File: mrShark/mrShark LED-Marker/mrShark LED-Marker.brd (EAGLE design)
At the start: 26 x 31 mm, 38 parts, among them CON1 DF12-20DS, IC1 PCA9552PW

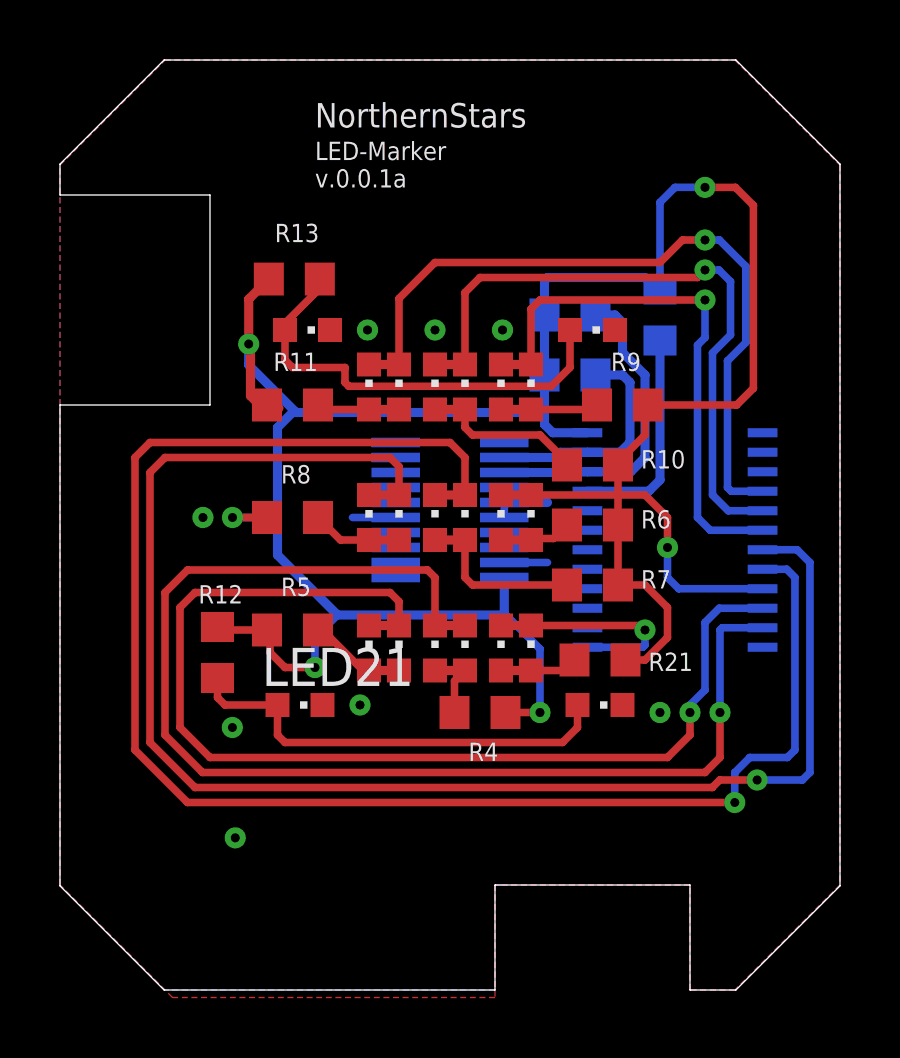
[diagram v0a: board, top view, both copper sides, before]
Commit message: Updated LED-marker to version 0.0.1
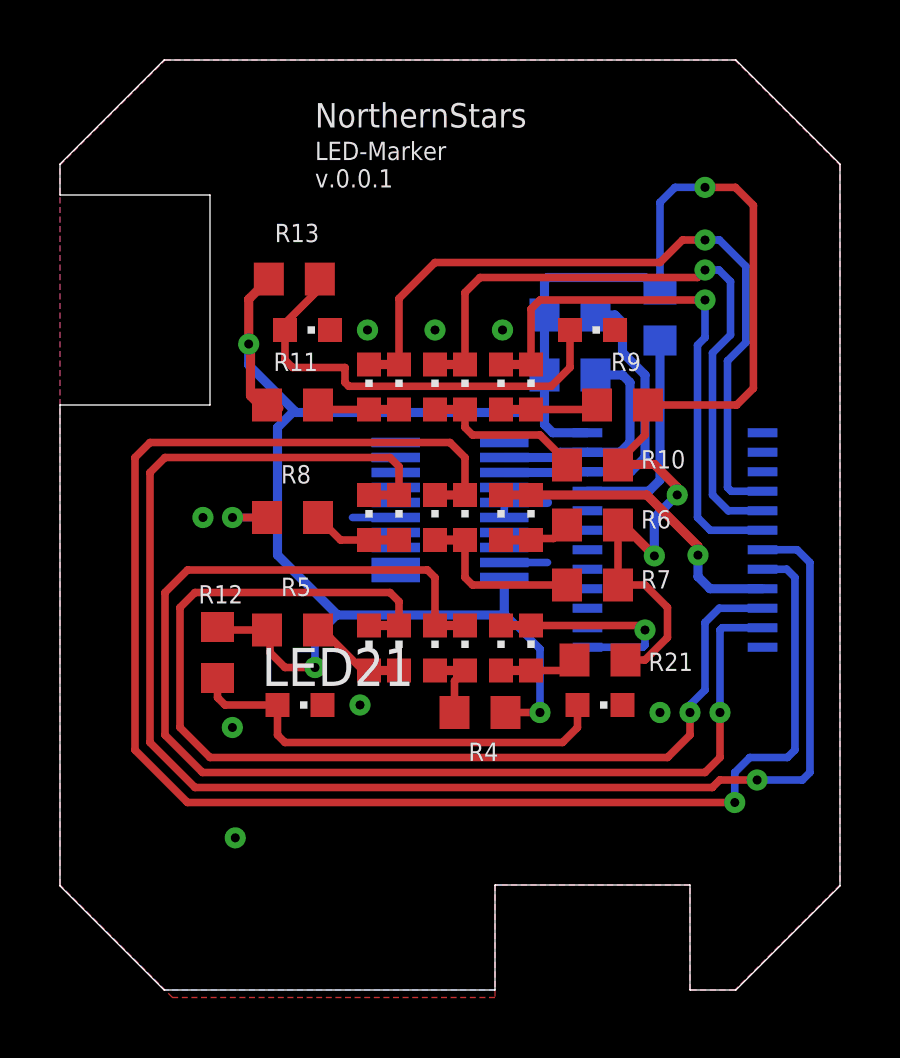
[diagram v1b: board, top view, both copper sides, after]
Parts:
- LED2: value (none) -> LW L283
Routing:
- net VCC: track 83.5 -> 88.0 mm, vias 5 -> 7
- net N$18: track 11.2 -> 10.6 mm
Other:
- board text added: "LED-Marker v.0.0.1"
- board text removed: "LED-Marker v.0.0.1a"
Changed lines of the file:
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@@
 <text x="8.5" y="28.25" size="0.8128" layer="25" font="vector" ratio="15">NorthernStars</text>
 <text x="8.5" y="26.25" size="0.6096" layer="25" font="vector" ratio="15">LED-Marker
-v.0.0.1a</text>
+v.0.0.1</text>
 <wire x1="5" y1="26" x2="5" y2="19" width="0" layer="20"/>
 <wire x1="0" y1="26" x2="5" y2="26" width="0" layer="20"/>
@@
 <attribute name="VALUE" x="12.205" y="18.33" size="1.27" layer="27" rot="R90"/>
 </element>
-<element name="LED2" library="led" package="CHIPLED_0603" value="" x="11.3" y="19.6" smashed="yes">
+<element name="LED2" library="led" package="CHIPLED_0603" value="LW L283" x="11.3" y="19.6" smashed="yes">
 <attribute name="VALUE" x="13.205" y="18.33" size="1.27" layer="27" rot="R90"/>
 </element>
@@
 <wire x1="5.75" y1="15.25" x2="7.25" y2="15.25" width="0.254" layer="16"/>
 <via x="6.29" y="21.032" extent="1-16" drill="0.3" shape="octagon"/>
-<wire x1="18.6" y1="15" x2="18.6" y2="17" width="0.254" layer="1"/>
 <wire x1="18.6" y1="13" x2="18.6" y2="15" width="0.254" layer="1"/>
 <via x="21.5" y="26.254" extent="1-16" drill="0.3" shape="octagon"/>
@@
 <wire x1="23.114" y1="25.654" x2="22.514" y2="26.254" width="0.254" layer="1"/>
 <wire x1="21.5" y1="26.254" x2="22.514" y2="26.254" width="0.254" layer="1"/>
+<wire x1="18.6" y1="15" x2="18.782" y2="15" width="0.3048" layer="1"/>
+<wire x1="18.782" y1="15" x2="19.812" y2="13.97" width="0.3048" layer="1"/>
+<via x="19.812" y="13.97" extent="1-16" drill="0.3" shape="octagon"/>
+<wire x1="19.812" y1="13.97" x2="19.812" y2="15.24" width="0.3048" layer="16"/>
+<wire x1="19.812" y1="15.24" x2="20.574" y2="16.002" width="0.3048" layer="16"/>
+<via x="20.574" y="16.002" extent="1-16" drill="0.3" shape="octagon"/>
+<wire x1="20.574" y1="16.002" x2="20.574" y2="16.256" width="0.3048" layer="1"/>
+<wire x1="20.574" y1="16.256" x2="19.812" y2="17.018" width="0.3048" layer="1"/>
+<wire x1="19.812" y1="17.018" x2="18.618" y2="17.018" width="0.3048" layer="1"/>
+<wire x1="18.618" y1="17.018" x2="18.6" y2="17" width="0.3048" layer="1"/>
 </signal>
 <signal name="GND">
@@
 <contactref element="LED11" pad="C"/>
 <wire x1="14.7" y1="16" x2="15.7" y2="16" width="0.3048" layer="1"/>
-<wire x1="15.7" y1="16" x2="19.5" y2="16" width="0.254" layer="1"/>
-<via x="20.25" y="14.25" extent="1-16" drill="0.3" shape="octagon"/>
-<wire x1="20.25" y1="13.25" x2="20.625" y2="12.875" width="0.254" layer="16"/>
-<wire x1="23.4178" y1="12.875" x2="20.625" y2="12.875" width="0.254" layer="16"/>
-<wire x1="20.25" y1="13.25" x2="20.25" y2="14.25" width="0.254" layer="16"/>
-<wire x1="20.25" y1="14.25" x2="20.25" y2="15.25" width="0.254" layer="1"/>
-<wire x1="20.25" y1="15.25" x2="19.5" y2="16" width="0.254" layer="1"/>
+<via x="21.266" y="13.996" extent="1-16" drill="0.3" shape="octagon"/>
+<wire x1="23.4178" y1="12.875" x2="21.669" y2="12.875" width="0.3048" layer="16"/>
+<wire x1="15.7" y1="16" x2="19.56" y2="16" width="0.3048" layer="1"/>
+<wire x1="19.56" y1="16" x2="21.266" y2="14.294" width="0.3048" layer="1"/>
+<wire x1="21.266" y1="14.294" x2="21.266" y2="13.996" width="0.3048" layer="1"/>
+<wire x1="21.669" y1="12.875" x2="21.266" y2="13.278" width="0.3048" layer="16"/>
+<wire x1="21.266" y1="13.278" x2="21.266" y2="13.996" width="0.3048" layer="16"/>
 </signal>
 <signal name="N$19">

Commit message: Updated LED-marker
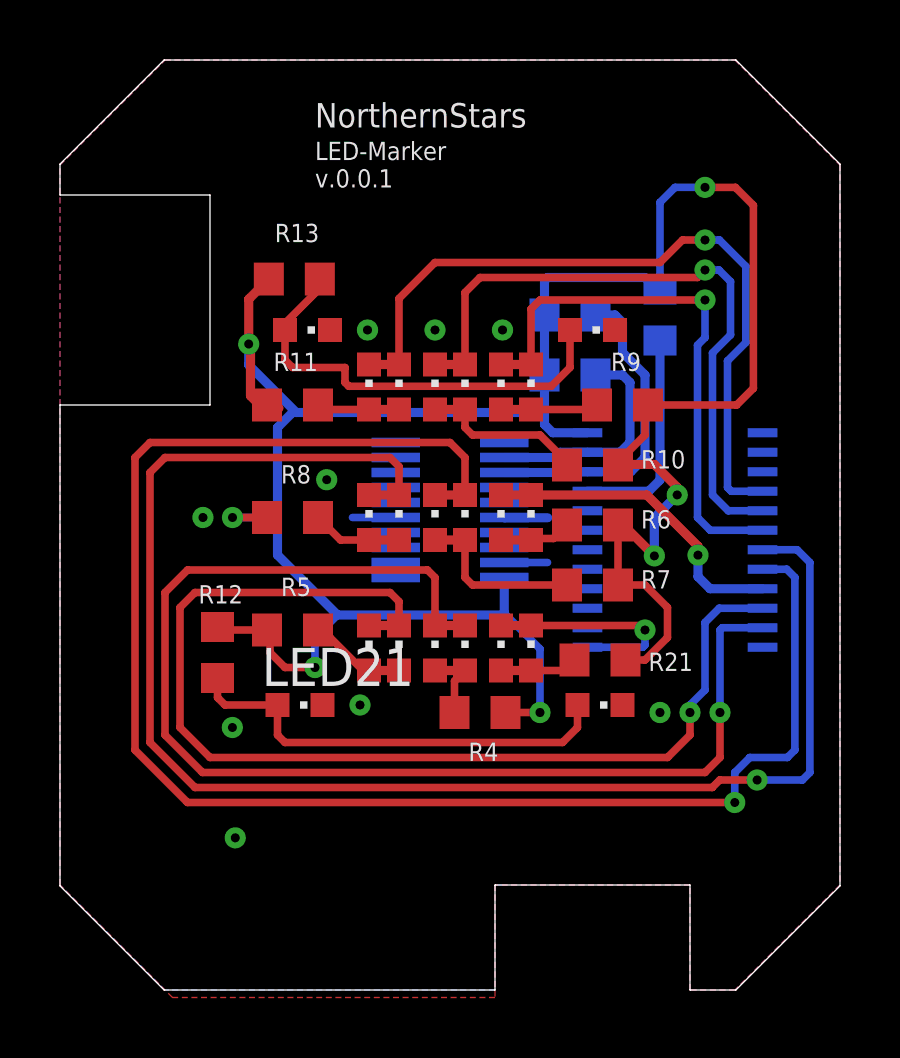
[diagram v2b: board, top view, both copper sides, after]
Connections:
- net GND: no longer CON1.16
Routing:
- net GND: track 4.82 -> 4.33 mm, vias 8 -> 9
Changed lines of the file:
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@@
 <signal name="GND">
 <contactref element="CON1" pad="15"/>
-<contactref element="CON1" pad="16"/>
 <contactref element="CON1" pad="12"/>
 <contactref element="CON1" pad="6"/>
@@
 <vertex x="3.75" y="-0.75"/>
 </polygon>
-<wire x1="14.81" y1="15.75" x2="16.25" y2="15.75" width="0.3048" layer="16"/>
 <contactref element="LED20" pad="C"/>
 <contactref element="LED19" pad="C"/>
@@
 <contactref element="LED21" pad="C"/>
 <wire x1="14.81" y1="13.75" x2="16.25" y2="13.75" width="0.254" layer="16"/>
-<wire x1="14.81" y1="15.25" x2="14.81" y2="15.75" width="0.254" layer="16"/>
 <via x="10.25" y="21.5" extent="1-16" drill="0.3" shape="octagon"/>
 <via x="10" y="9" extent="1-16" drill="0.3" shape="octagon"/>
@@
 <via x="5.746" y="8.25" extent="1-16" drill="0.3" shape="octagon"/>
 <via x="5.842" y="4.572" extent="1-16" drill="0.3" shape="octagon"/>
-<wire x1="11.19" y1="15.25" x2="14.81" y2="15.25" width="0" layer="19" extent="16-16"/>
+<wire x1="14.81" y1="15.25" x2="14.82" y2="15.24" width="0.3048" layer="16"/>
+<wire x1="14.82" y1="15.24" x2="16.256" y2="15.24" width="0.3048" layer="16"/>
+<via x="8.89" y="16.51" extent="1-16" drill="0.3" shape="octagon"/>
 </signal>
 <signal name="INT1">

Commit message: Added switchable position lights
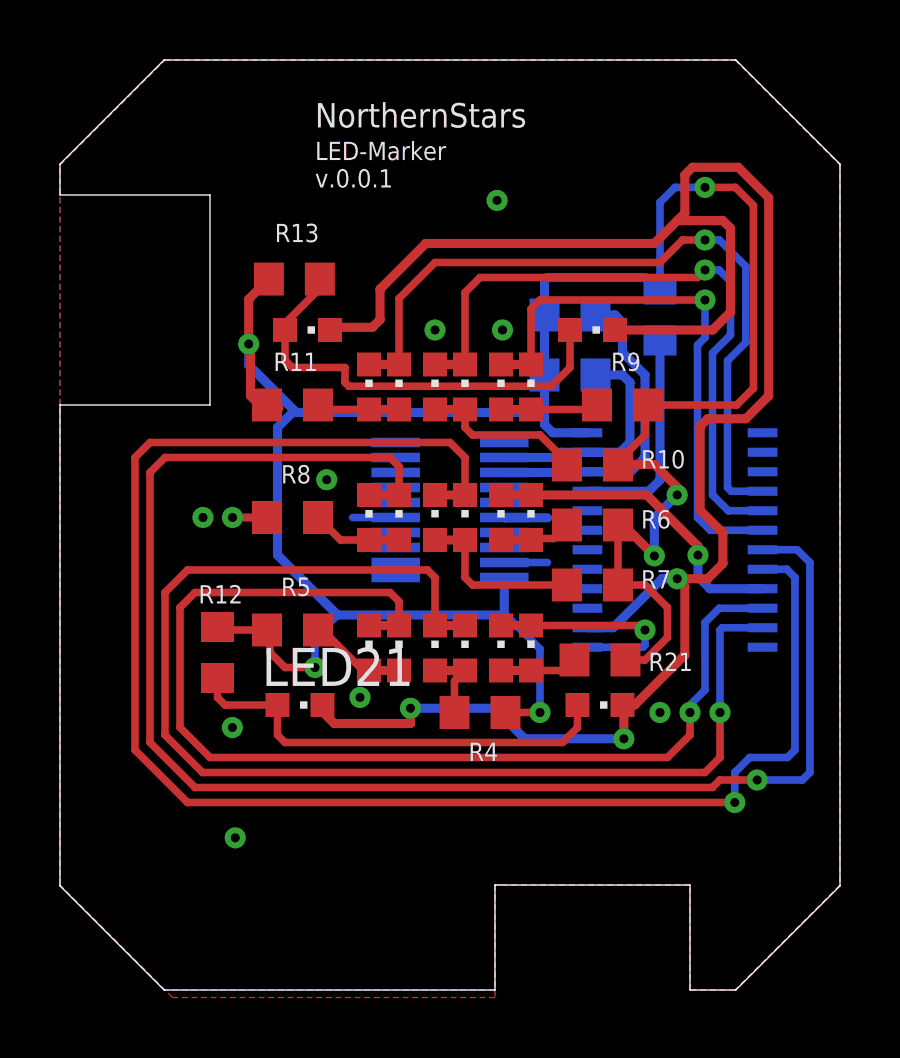
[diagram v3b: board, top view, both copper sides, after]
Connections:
- new net POS_LIGHT: IC1.14, LED19.C, LED20.C, LED21.C, LED22.C
- net GND: no longer LED19.C, LED20.C, LED21.C, LED22.C
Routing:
- net POS_LIGHT: track 0.00 -> 64.9 mm, vias 0 -> 3
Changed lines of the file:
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@@
 <vertex x="3.75" y="-0.75"/>
 </polygon>
-<contactref element="LED20" pad="C"/>
-<contactref element="LED19" pad="C"/>
-<contactref element="LED22" pad="C"/>
-<contactref element="LED21" pad="C"/>
 <wire x1="14.81" y1="13.75" x2="16.25" y2="13.75" width="0.254" layer="16"/>
-<via x="10.25" y="21.5" extent="1-16" drill="0.3" shape="octagon"/>
-<via x="10" y="9" extent="1-16" drill="0.3" shape="octagon"/>
+<via x="14.568" y="25.818" extent="1-16" drill="0.3" shape="octagon"/>
+<via x="10" y="9.254" extent="1-16" drill="0.3" shape="octagon"/>
 <wire x1="11.19" y1="15.25" x2="9.75" y2="15.25" width="0.254" layer="16"/>
 <via x="20" y="8.75" extent="1-16" drill="0.3" shape="octagon"/>
@@
 <wire x1="8.662" y1="22.886" x2="8.662" y2="23.198" width="0.254" layer="1"/>
 </signal>
+<signal name="POS_LIGHT">
+<contactref element="IC1" pad="14"/>
+<contactref element="LED20" pad="C"/>
+<contactref element="LED19" pad="C"/>
+<contactref element="LED22" pad="C"/>
+<contactref element="LED21" pad="C"/>
+<wire x1="17.5822" y1="11.575" x2="18.433" y2="11.575" width="0.3048" layer="16"/>
+<wire x1="18.433" y1="11.575" x2="20.066" y2="13.208" width="0.3048" layer="16"/>
+<wire x1="8.75" y1="9" x2="8.75" y2="8.776" width="0.3048" layer="1"/>
+<wire x1="8.75" y1="8.776" x2="9.144" y2="8.382" width="0.3048" layer="1"/>
+<wire x1="9.144" y1="8.382" x2="11.684" y2="8.382" width="0.3048" layer="1"/>
+<wire x1="11.684" y1="8.382" x2="11.684" y2="8.89" width="0.3048" layer="1"/>
+<via x="11.684" y="8.89" extent="1-16" drill="0.3" shape="octagon"/>
+<wire x1="11.684" y1="8.89" x2="14.478" y2="8.89" width="0.3048" layer="16"/>
+<wire x1="14.478" y1="8.89" x2="15.494" y2="7.874" width="0.3048" layer="16"/>
+<wire x1="15.494" y1="7.874" x2="18.796" y2="7.874" width="0.3048" layer="16"/>
+<via x="18.796" y="7.874" extent="1-16" drill="0.3" shape="octagon"/>
+<wire x1="18.796" y1="7.874" x2="18.796" y2="8.954" width="0.3048" layer="1"/>
+<wire x1="18.796" y1="8.954" x2="18.75" y2="9" width="0.3048" layer="1"/>
+<wire x1="18.5" y1="21.5" x2="21.754" y2="21.5" width="0.3048" layer="1"/>
+<wire x1="21.754" y1="21.5" x2="22.352" y2="22.098" width="0.3048" layer="1"/>
+<wire x1="22.352" y1="22.098" x2="22.352" y2="24.892" width="0.3048" layer="1"/>
+<wire x1="22.352" y1="24.892" x2="22.098" y2="25.146" width="0.3048" layer="1"/>
+<wire x1="22.098" y1="25.146" x2="20.574" y2="25.146" width="0.3048" layer="1"/>
+<wire x1="20.574" y1="25.146" x2="19.812" y2="24.384" width="0.3048" layer="1"/>
+<wire x1="19.812" y1="24.384" x2="12.192" y2="24.384" width="0.3048" layer="1"/>
+<wire x1="12.192" y1="24.384" x2="10.668" y2="22.86" width="0.3048" layer="1"/>
+<wire x1="10.668" y1="22.86" x2="10.668" y2="21.844" width="0.3048" layer="1"/>
+<wire x1="10.668" y1="21.844" x2="10.414" y2="21.59" width="0.3048" layer="1"/>
+<wire x1="10.414" y1="21.59" x2="9.09" y2="21.59" width="0.3048" layer="1"/>
+<wire x1="9.09" y1="21.59" x2="9" y2="21.5" width="0.3048" layer="1"/>
+<wire x1="22.098" y1="13.716" x2="22.098" y2="14.732" width="0.3048" layer="1"/>
+<wire x1="22.098" y1="14.732" x2="21.336" y2="15.494" width="0.3048" layer="1"/>
+<wire x1="21.336" y1="15.494" x2="21.336" y2="18.288" width="0.3048" layer="1"/>
+<wire x1="21.336" y1="18.288" x2="21.59" y2="18.542" width="0.3048" layer="1"/>
+<wire x1="21.59" y1="18.542" x2="22.86" y2="18.542" width="0.3048" layer="1"/>
+<wire x1="22.86" y1="18.542" x2="23.622" y2="19.304" width="0.3048" layer="1"/>
+<wire x1="23.622" y1="19.304" x2="23.622" y2="25.908" width="0.3048" layer="1"/>
+<wire x1="23.622" y1="25.908" x2="22.606" y2="26.924" width="0.3048" layer="1"/>
+<wire x1="22.606" y1="26.924" x2="21.082" y2="26.924" width="0.3048" layer="1"/>
+<wire x1="21.082" y1="26.924" x2="20.828" y2="26.67" width="0.3048" layer="1"/>
+<wire x1="20.828" y1="26.67" x2="20.828" y2="25.4" width="0.3048" layer="1"/>
+<wire x1="20.828" y1="25.4" x2="20.574" y2="25.146" width="0.3048" layer="1"/>
+<wire x1="22.098" y1="13.716" x2="21.59" y2="13.208" width="0.3048" layer="1"/>
+<wire x1="21.59" y1="13.208" x2="20.574" y2="13.208" width="0.3048" layer="1"/>
+<via x="20.574" y="13.208" extent="1-16" drill="0.3" shape="octagon"/>
+<wire x1="20.574" y1="13.208" x2="20.066" y2="13.208" width="0.3048" layer="16"/>
+<wire x1="18.75" y1="9" x2="19.16" y2="9" width="0.3048" layer="1"/>
+<wire x1="19.16" y1="9" x2="20.828" y2="10.668" width="0.3048" layer="1"/>
+<wire x1="20.828" y1="10.668" x2="20.828" y2="12.954" width="0.3048" layer="1"/>
+<wire x1="20.828" y1="12.954" x2="20.574" y2="13.208" width="0.3048" layer="1"/>
+</signal>
 </signals>
